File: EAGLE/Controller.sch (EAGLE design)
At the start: 39 parts, among them IC1 TPS77033, IC2 TPS77033, Q1 200mA/40V, Q2 200mA/40V, Q3 2N3906, U1 ATMEGA328P_TQFP, U2 MCP73831, Y1 16MHz

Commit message: Pre Layout
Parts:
- removed Q1, Q2: 200mA/40V, SparkFun-DiscreteSemi:TRANS_NPN-2N3904
- removed Q3: 2N3906, transistor-pnp:2N3906
- removed R4: (no value), pot:TRIM_EU-B64Y
- added R11: (no value), pot-vitrohm:PC25
- added T1, T2: (no value), transistor-neu-to92:MMBT3904LT1-NPN-SOT23-BEC
- added T3: MMBT3906LT1SMD, transistor-pnp:MMBT3906LT1SMD
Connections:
- new net N$18: LED2.C, R9.1
- net GND: now also R11.A, T1.E, T2.E; no longer Q1.E, Q2.E, R4.A
- net N$1: now also T2.C, T3.B; no longer Q2.C, Q3.B
- net N$2: now also R11.S, T1.B; no longer Q1.B, R4.S
- net N$4: now also T1.C, T2.B, T3.C; no longer Q1.C, Q2.B, Q3.C
- net N$5: now also T3.E; no longer Q3.E
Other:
- moved on the sheet: C9, R9

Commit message: pre-Layout
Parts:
- removed J2: (no value), SparkFun-Connectors:JST_2MM_MALE
- added C11, C12: 0.1uF, SparkFun-Capacitors:0.1UF-0603-25V-5%
- added FB4, FB5: 30Ω/1.8A, SparkFun-Coils:FERRITE_BEAD-0603
- added JP1: (no value), pinhead:PINHD-1X10/90
- added JP2: (no value), pinhead:PINHD-1X4
- added JP3: (no value), pinhead:PINHD-1X2/90
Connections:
- removed net N$14: J2.+, S1.P
- removed net OELD_MOSI: U1.PB3(MOSI/OC2)
- removed net OLED_MISO: U1.PB4(MISO)
- new net CAM_GND: C11.2, JP2.4
- new net CAM_VCC: C11.1, FB4.2, JP2.1
- new net LIPO_POS: JP3.1, S1.P
- new net OLED_DC: JP1.6, U1.PB0(ICP)
- new net OLED_GND: C12.2, JP1.1
- new net OLED_MOSI: JP1.8, U1.PB3(MOSI/OC2)
- new net OLED_OC: JP1.4, U1.PB2(SS/OC1B)
- new net OLED_RESET: JP1.5, U1.PB1(OC1A)
- new net OLED_VCC: C12.1, FB5.2, JP1.2
- net CAM_SCL: now also JP2.3
- net CAM_SDA: now also JP2.2
- net GND: now also JP3.2; no longer J2.-
- net N$8: now also FB4.1, FB5.1
- net OLED_SCK: now also JP1.7
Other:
- note added: "Camera Connection Pins"
- note added: "OLED Connection Pins"
- moved on the sheet: C1, C10, C2, C3, C9, FB1, FB2, FB3, J1, LED1, LED2, LED3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

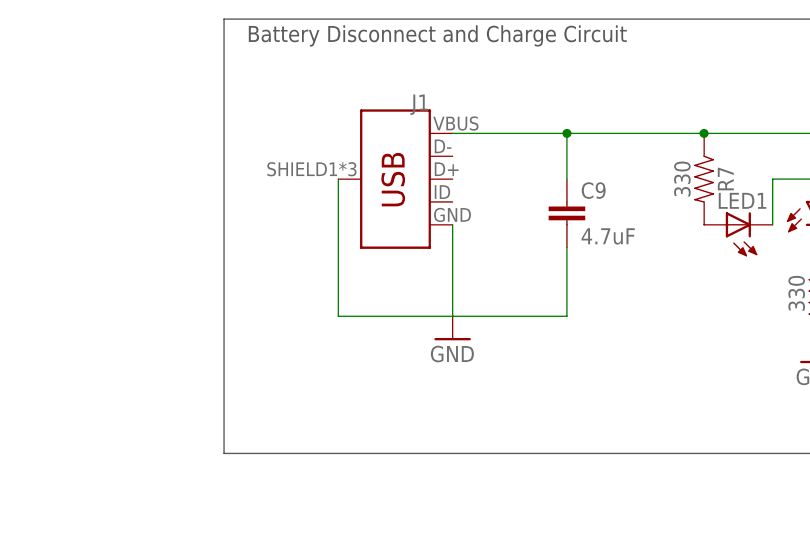
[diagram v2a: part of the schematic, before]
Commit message: altered board to fit OSH DRS
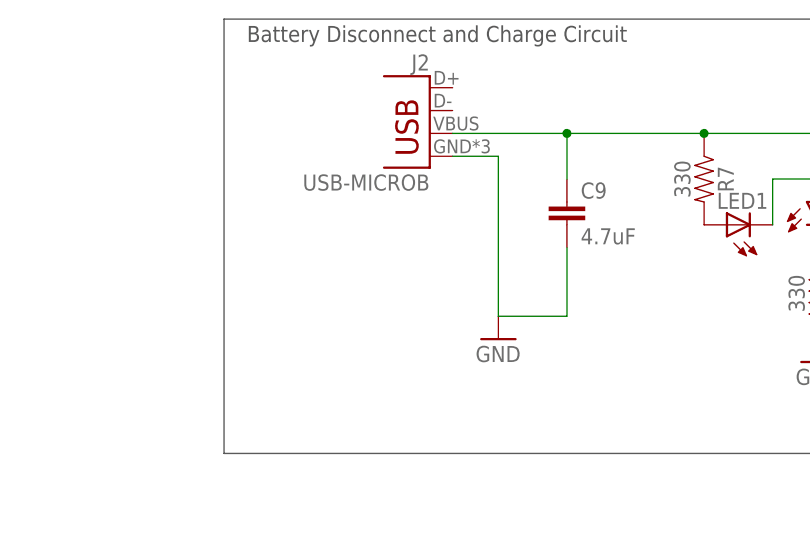
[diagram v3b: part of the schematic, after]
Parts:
- removed J1: (no value), SparkFun-Connectors:USB_MICRO-B_FEMALE-SMT
- added J2: USB-MICROB, SparkFun-Retired:USB-MICROB
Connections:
- net GND: now also J2.GND; no longer J1.GND, J1.SHIELD
- net N$11: now also J2.VBUS; no longer J1.VBUS
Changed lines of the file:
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@@
 <part name="GND5" library="supply1" library_urn="urn:adsk.eagle:library:371" deviceset="GND" device=""/>
 <part name="GND6" library="supply1" library_urn="urn:adsk.eagle:library:371" deviceset="GND" device=""/>
-<part name="J1" library="SparkFun-Connectors" library_urn="urn:adsk.eagle:library:513" deviceset="USB_MICRO-B" device="_FEMALE-SMT" package3d_urn="urn:adsk.eagle:package:38238/1"/>
 <part name="GND7" library="supply1" library_urn="urn:adsk.eagle:library:371" deviceset="GND" device=""/>
 <part name="U2" library="SparkFun-IC-Power" library_urn="urn:adsk.eagle:library:526" deviceset="MCP73831" device="" package3d_urn="urn:adsk.eagle:package:39060/1"/>
@@
 <part name="JP3" library="pinhead" library_urn="urn:adsk.eagle:library:325" deviceset="PINHD-1X2" device="/90" package3d_urn="urn:adsk.eagle:package:22437/2"/>
 <part name="JP1" library="pinhead" library_urn="urn:adsk.eagle:library:325" deviceset="PINHD-1X10" device="/90" package3d_urn="urn:adsk.eagle:package:22408/2"/>
+<part name="J2" library="SparkFun-Retired" library_urn="urn:adsk.eagle:library:533" deviceset="USB" device="-MICROB"/>
 </parts>
 <sheets>
@@
 <instance part="GND5" gate="1" x="81.28" y="58.42"/>
 <instance part="GND6" gate="1" x="215.9" y="93.98"/>
-<instance part="J1" gate="G$1" x="93.98" y="215.9" rot="MR0"/>
-<instance part="GND7" gate="1" x="99.06" y="198.12"/>
+<instance part="GND7" gate="1" x="104.14" y="198.12"/>
 <instance part="U2" gate="G$1" x="154.94" y="218.44"/>
 <instance part="C9" gate="G$1" x="111.76" y="210.82"/>
@@
 <instance part="JP3" gate="G$1" x="210.82" y="205.74"/>
 <instance part="JP1" gate="A" x="353.06" y="139.7"/>
+<instance part="J2" gate="G$1" x="96.52" y="218.44" rot="MR0"/>
 </instances>
 <busses>
@@
 <segment>
 <pinref part="GND7" gate="1" pin="GND"/>
-<pinref part="J1" gate="G$1" pin="SHIELD"/>
-<wire x1="86.36" y1="215.9" x2="86.36" y2="200.66" width="0.1524" layer="91"/>
-<wire x1="99.06" y1="200.66" x2="86.36" y2="200.66" width="0.1524" layer="91"/>
-<pinref part="J1" gate="G$1" pin="GND"/>
-<wire x1="99.06" y1="210.82" x2="99.06" y2="200.66" width="0.1524" layer="91"/>
+<wire x1="104.14" y1="218.44" x2="104.14" y2="200.66" width="0.1524" layer="91"/>
 <pinref part="C9" gate="G$1" pin="2"/>
 <wire x1="111.76" y1="208.28" x2="111.76" y2="200.66" width="0.1524" layer="91"/>
-<wire x1="111.76" y1="200.66" x2="99.06" y2="200.66" width="0.1524" layer="91"/>
+<wire x1="111.76" y1="200.66" x2="104.14" y2="200.66" width="0.1524" layer="91"/>
+<pinref part="J2" gate="G$1" pin="GND"/>
+<wire x1="104.14" y1="218.44" x2="99.06" y2="218.44" width="0.1524" layer="91"/>
 </segment>
 <segment>
@@
 <segment>
 <pinref part="R7" gate="G$1" pin="1"/>
-<pinref part="J1" gate="G$1" pin="VBUS"/>
 <wire x1="127" y1="220.98" x2="111.76" y2="220.98" width="0.1524" layer="91"/>
 <pinref part="C9" gate="G$1" pin="1"/>
@@
 <wire x1="127" y1="220.98" x2="144.78" y2="220.98" width="0.1524" layer="91"/>
 <junction x="127" y="220.98"/>
-</segment>
-</net>
+<pinref part="J2" gate="G$1" pin="VBUS"/>
+</segment>
+</net>
